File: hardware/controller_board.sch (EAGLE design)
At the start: 123 parts, among them J1 FRSKY-GIMBAL-FRYSKY, J11 USB-MICROA-AMPHENOL-10118192-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, J2 FRSKY-GIMBAL-FRYSKY, J3 USB-MINIB-EDAC-690-005-299-043, J4 AVR_SPI_PRG_6NS, J5 JUMPER-SMT_2_NC_PASTE_NO-SILK, J8 FRSKY-GIMBAL-2X-SERVO, J9 FRSKY-GIMBAL-2X-SERVO, P1 TEST-POINT, P2 TEST-POINT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

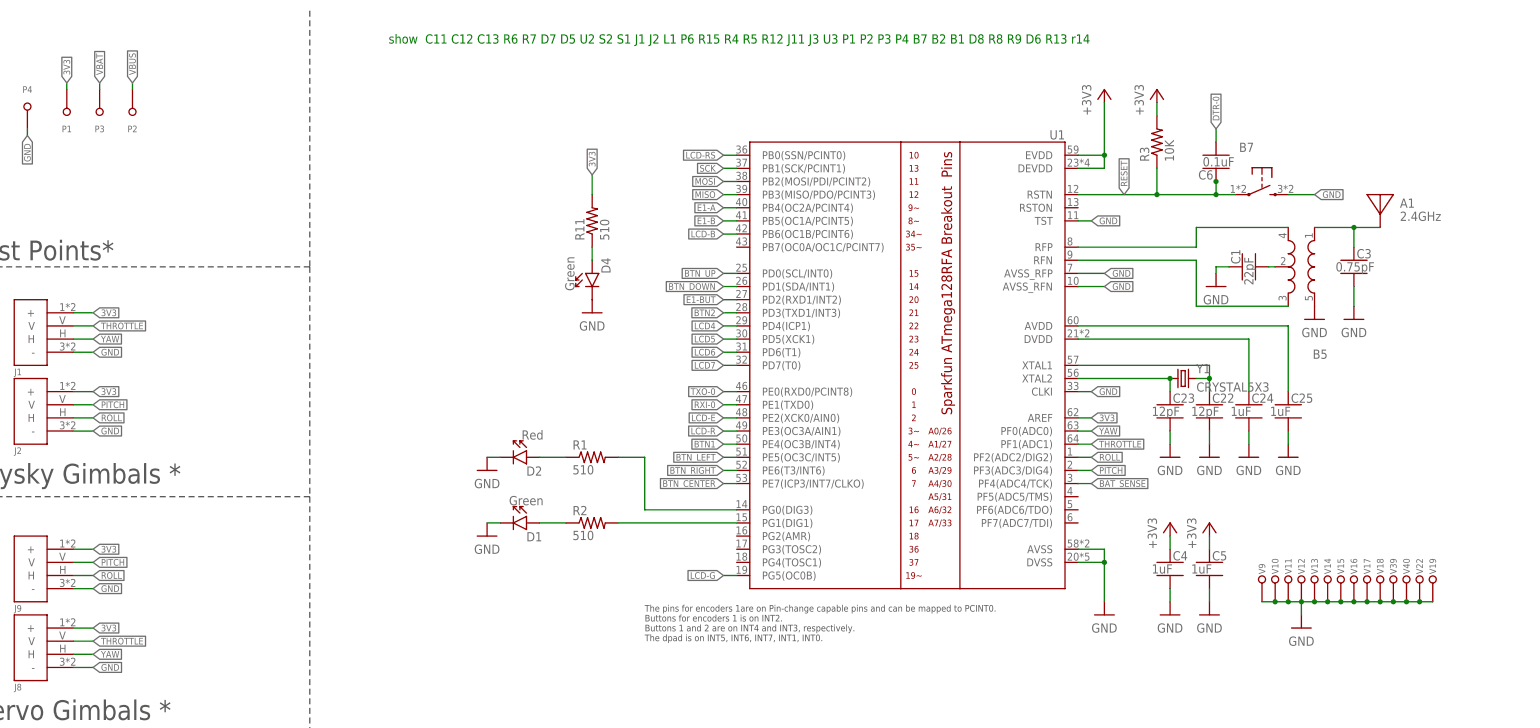
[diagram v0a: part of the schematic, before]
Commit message: added configuration jumpers for AREF
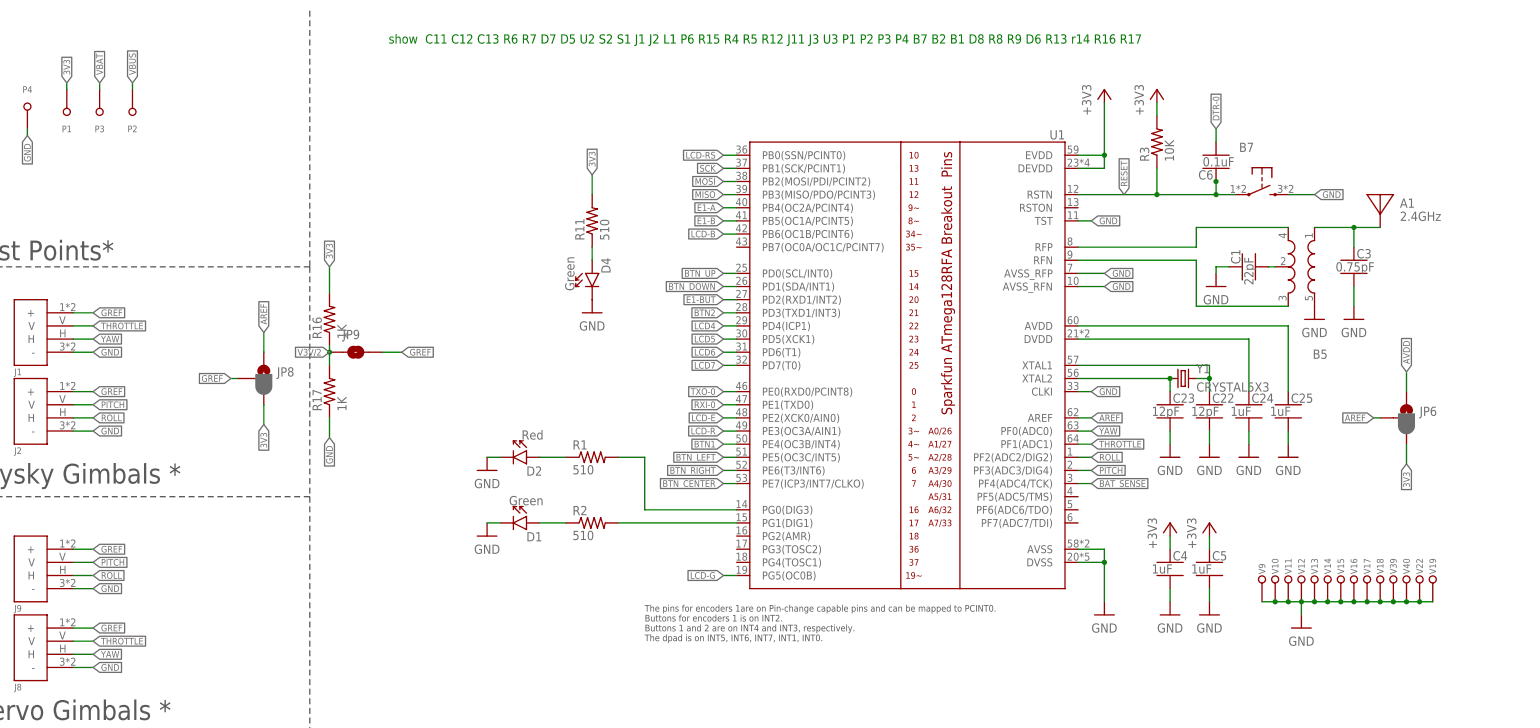
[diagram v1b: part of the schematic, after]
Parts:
- added JP6, JP8: JUMPER-SMT_3_1-NC_PASTE_NO-SILK, RemoteParts:JUMPER-SMT_3_1-NC_PASTE_NO-SILK
- added JP9: JUMPER-SMT_2_NO_NO-SILK, RemoteParts:JUMPER-SMT_2_NO_NO-SILK
- added R16, R17: 1K, quadparts_prebuilt:RESISTOR_SMD-2012-0805-1K
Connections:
- new net AREF: JP6.2, JP8.1, U1.AREF
- new net AVDD: JP6.1
- new net GREF: J1.+, J2.+, J8.+, J9.+, JP8.2, JP9.2
- new net V3V/2: JP9.1, R16.1, R17.2
- net 3V3: now also JP6.3, JP8.3, R16.2; no longer J1.+, J2.+, J8.+, J9.+, U1.AREF
- net GND: now also R17.1
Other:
- note added: "show C11 C12 C13 R6 R7 D7 D5 U2 S2 S1 J1 J2 L1 P6 R15 R4 R5 R12 J11 J3 U3 P1 P2 P3 P4 B7 B2 B1 D8 R8 R9 D6 R13 r14 R16 R17"
- note removed: "show C11 C12 C13 R6 R7 D7 D5 U2 S2 S1 J1 J2 L1 P6 R15 R4 R5 R12 J11 J3 U3 P1 P2 P3 P4 B7 B2 B1 D8 R8 R9 D6 R13 r14"
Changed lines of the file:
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@@
 <setting verticaltext="up"/>
 </settings>
-<grid distance="0.1" unitdist="inch" unit="inch" style="lines" multiple="1" display="no" altdistance="0.01" altunitdist="inch" altunit="inch"/>
+<grid distance="0.05" unitdist="inch" unit="inch" style="lines" multiple="1" display="no" altdistance="0.01" altunitdist="inch" altunit="inch"/>
 <layers>
 <layer number="99" name="SpiceOrder" color="7" fill="1" visible="no" active="no"/>
@@
 <part name="E1" library="RemoteParts" deviceset="ROTARY-ENCODER-W/BUTTON" device="-BOURNS-PEC12R-30MM"/>
 <part name="J5" library="RemoteParts" deviceset="JUMPER-SMT_2_NC_PASTE" device="_NO-SILK"/>
+<part name="JP6" library="RemoteParts" deviceset="JUMPER-SMT_3_1-NC_PASTE" device="_NO-SILK"/>
+<part name="JP8" library="RemoteParts" deviceset="JUMPER-SMT_3_1-NC_PASTE" device="_NO-SILK"/>
+<part name="R16" library="quadparts_prebuilt" deviceset="RESISTOR_" device="SMD-2012-0805-1K" value="1K"/>
+<part name="R17" library="quadparts_prebuilt" deviceset="RESISTOR_" device="SMD-2012-0805-1K" value="1K"/>
+<part name="JP9" library="RemoteParts" deviceset="JUMPER-SMT_2_NO" device="_NO-SILK"/>
 </parts>
 <sheets>
@@
 <wire x1="72.39" y1="96.52" x2="3.81" y2="95.25" width="0.1524" layer="97" style="longdash"/>
 <text x="6.35" y="97.79" size="3.81" layer="97">150mA 3.3V Regulator *</text>
-<text x="87.63" y="269.24" size="1.778" layer="91">show  C11 C12 C13 R6 R7 D7 D5 U2 S2 S1 J1 J2 L1 P6 R15 R4 R5 R12 J11 J3 U3 P1 P2 P3 P4 B7 B2 B1 D8 R8 R9 D6 R13 r14</text>
+<text x="87.63" y="269.24" size="1.778" layer="91">show  C11 C12 C13 R6 R7 D7 D5 U2 S2 S1 J1 J2 L1 P6 R15 R4 R5 R12 J11 J3 U3 P1 P2 P3 P4 B7 B2 B1 D8 R8 R9 D6 R13 r14 R16 R17</text>
 <text x="7.62" y="132.08" size="1.778" layer="97">C10 is the input cap (shared with lipo charger)</text>
 </plain>
@@
 <instance part="E1" gate="G$1" x="388.62" y="267.97"/>
 <instance part="J5" gate="G$1" x="21.59" y="107.95"/>
+<instance part="JP6" gate="G$1" x="284.48" y="196.85"/>
+<instance part="JP8" gate="G$1" x="63.5" y="204.47"/>
+<instance part="R16" gate="G$1" x="76.2" y="215.9" rot="R90"/>
+<instance part="R17" gate="G$1" x="76.2" y="201.93" rot="R90"/>
+<instance part="JP9" gate="G$1" x="81.28" y="209.55"/>
 </instances>
 <busses>
@@
 <label x="300.99" y="68.58" size="1.27" layer="95" xref="yes"/>
 </segment>
+<segment>
+<pinref part="R17" gate="G$1" pin="1"/>
+<wire x1="76.2" y1="196.85" x2="76.2" y2="193.04" width="0.1524" layer="91"/>
+<label x="76.2" y="193.04" size="1.27" layer="95" rot="R270" xref="yes"/>
+</segment>
 </net>
 <net name="BTN1" class="0">
@@
 </segment>
 <segment>
-<pinref part="U1" gate="G$1" pin="AREF"/>
-<wire x1="223.52" y1="196.85" x2="220.98" y2="196.85" width="0.1524" layer="91"/>
-<label x="223.52" y="196.85" size="1.27" layer="95" xref="yes"/>
-</segment>
-<segment>
 <wire x1="25.4" y1="261.62" x2="25.4" y2="260.35" width="0.1524" layer="91"/>
 <label x="25.4" y="261.62" size="1.27" layer="95" rot="R90" xref="yes"/>
 <pinref part="P1" gate="G$1" pin="T"/>
-</segment>
-<segment>
-<pinref part="J1" gate="G$1" pin="+"/>
-<wire x1="26.67" y1="217.17" x2="30.48" y2="217.17" width="0.1524" layer="91"/>
-<label x="30.48" y="217.17" size="1.27" layer="95" xref="yes"/>
-</segment>
-<segment>
-<pinref part="J8" gate="G$1" pin="+"/>
-<wire x1="26.67" y1="156.21" x2="30.48" y2="156.21" width="0.1524" layer="91"/>
-<label x="30.48" y="156.21" size="1.27" layer="95" xref="yes"/>
-</segment>
-<segment>
-<pinref part="J2" gate="G$1" pin="+"/>
-<wire x1="26.67" y1="201.93" x2="30.48" y2="201.93" width="0.1524" layer="91"/>
-<label x="30.48" y="201.93" size="1.27" layer="95" xref="yes"/>
-</segment>
-<segment>
-<pinref part="J9" gate="G$1" pin="+"/>
-<wire x1="26.67" y1="171.45" x2="30.48" y2="171.45" width="0.1524" layer="91"/>
-<label x="30.48" y="171.45" size="1.27" layer="95" xref="yes"/>
 </segment>
 <segment>
@@
 <wire x1="289.56" y1="73.66" x2="300.99" y2="73.66" width="0.1524" layer="91"/>
 <label x="300.99" y="73.66" size="1.27" layer="95" xref="yes"/>
+</segment>
+<segment>
+<pinref part="JP6" gate="G$1" pin="3"/>
+<wire x1="284.48" y1="191.77" x2="284.48" y2="187.96" width="0.1524" layer="91"/>
+<label x="284.48" y="187.96" size="1.27" layer="95" rot="R270" xref="yes"/>
+</segment>
+<segment>
+<pinref part="JP8" gate="G$1" pin="3"/>
+<wire x1="63.5" y1="199.39" x2="63.5" y2="195.58" width="0.1524" layer="91"/>
+<label x="63.5" y="195.58" size="1.27" layer="95" rot="R270" xref="yes"/>
+</segment>
+<segment>
+<pinref part="R16" gate="G$1" pin="2"/>
+<wire x1="76.2" y1="220.98" x2="76.2" y2="226.06" width="0.1524" layer="91"/>
+<label x="76.2" y="226.06" size="1.27" layer="95" rot="R90" xref="yes"/>
 </segment>
 </net>
@@
 </segment>
 </net>
+<net name="AREF" class="0">
+<segment>
+<pinref part="JP6" gate="G$1" pin="2"/>
+<wire x1="279.4" y1="196.85" x2="278.13" y2="196.85" width="0.1524" layer="91"/>
+<label x="278.13" y="196.85" size="1.27" layer="95" rot="R180" xref="yes"/>
+</segment>
+<segment>
+<pinref part="U1" gate="G$1" pin="AREF"/>
+<wire x1="223.52" y1="196.85" x2="220.98" y2="196.85" width="0.1524" layer="91"/>
+<label x="223.52" y="196.85" size="1.27" layer="95" xref="yes"/>
+</segment>
+<segment>
+<pinref part="JP8" gate="G$1" pin="1"/>
+<wire x1="63.5" y1="209.55" x2="63.5" y2="213.36" width="0.1524" layer="91"/>
+<label x="63.5" y="213.36" size="1.27" layer="95" rot="R90" xref="yes"/>
+</segment>
+</net>
+<net name="AVDD" class="0">
+<segment>
+<pinref part="JP6" gate="G$1" pin="1"/>
+<wire x1="284.48" y1="201.93" x2="284.48" y2="205.74" width="0.1524" layer="91"/>
+<label x="284.48" y="205.74" size="1.27" layer="95" rot="R90" xref="yes"/>
+</segment>
+</net>
+<net name="GREF" class="0">
+<segment>
+<pinref part="JP8" gate="G$1" pin="2"/>
+<wire x1="58.42" y1="204.47" x2="57.15" y2="204.47" width="0.1524" layer="91"/>
+<label x="57.15" y="204.47" size="1.27" layer="95" rot="R180" xref="yes"/>
+</segment>
+<segment>
+<pinref part="J1" gate="G$1" pin="+"/>
+<wire x1="26.67" y1="217.17" x2="30.48" y2="217.17" width="0.1524" layer="91"/>
+<label x="30.48" y="217.17" size="1.27" layer="95" xref="yes"/>
+</segment>
+<segment>
+<pinref part="J2" gate="G$1" pin="+"/>
+<wire x1="26.67" y1="201.93" x2="30.48" y2="201.93" width="0.1524" layer="91"/>
+<label x="30.48" y="201.93" size="1.27" layer="95" xref="yes"/>
+</segment>
+<segment>
+<pinref part="J9" gate="G$1" pin="+"/>
+<wire x1="26.67" y1="171.45" x2="30.48" y2="171.45" width="0.1524" layer="91"/>
+<label x="30.48" y="171.45" size="1.27" layer="95" xref="yes"/>
+</segment>
+<segment>
+<pinref part="J8" gate="G$1" pin="+"/>
+<wire x1="26.67" y1="156.21" x2="30.48" y2="156.21" width="0.1524" layer="91"/>
+<label x="30.48" y="156.21" size="1.27" layer="95" xref="yes"/>
+</segment>
+<segment>
+<pinref part="JP9" gate="G$1" pin="2"/>
+<wire x1="86.36" y1="209.55" x2="90.17" y2="209.55" width="0.1524" layer="91"/>
+<label x="90.17" y="209.55" size="1.27" layer="95" xref="yes"/>
+</segment>
+</net>
+<net name="V3V/2" class="0">
+<segment>
+<pinref part="R16" gate="G$1" pin="1"/>
+<pinref part="R17" gate="G$1" pin="2"/>
+<wire x1="76.2" y1="210.82" x2="76.2" y2="209.55" width="0.1524" layer="91"/>
+<pinref part="JP9" gate="G$1" pin="1"/>
+<wire x1="76.2" y1="209.55" x2="76.2" y2="207.01" width="0.1524" layer="91"/>
+<junction x="76.2" y="209.55"/>
+<label x="76.2" y="209.55" size="1.27" layer="95" rot="R180" xref="yes"/>
+</segment>
+</net>

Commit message: test solder jumpers
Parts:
- added JP10, JP11, JP12, JP13, JP14, JP15, JP16, JP17: JUMPER-SMT_3_0-NC_PASTE, RemoteParts:JUMPER-SMT_3_0-NC_PASTE
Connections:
- new net N$1: JP10.3, JP11.1
- new net N$18: JP11.3, JP12.1
- new net N$25: JP12.3, JP13.1
- new net N$26: JP13.3, JP14.1
- new net N$27: JP14.3, JP15.1
- new net N$28: JP15.3, JP16.1
- new net N$29: JP16.3, JP17.1
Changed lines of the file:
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@@
 <part name="R17" library="quadparts_prebuilt" deviceset="RESISTOR_" device="SMD-2012-0805-1K" value="1K"/>
 <part name="JP9" library="RemoteParts" deviceset="JUMPER-SMT_2_NO" device="_NO-SILK"/>
+<part name="JP10" library="RemoteParts" deviceset="JUMPER-SMT_3_0-NC_PASTE" device=""/>
+<part name="JP11" library="RemoteParts" deviceset="JUMPER-SMT_3_0-NC_PASTE" device=""/>
+<part name="JP12" library="RemoteParts" deviceset="JUMPER-SMT_3_0-NC_PASTE" device=""/>
+<part name="JP13" library="RemoteParts" deviceset="JUMPER-SMT_3_0-NC_PASTE" device=""/>
+<part name="JP14" library="RemoteParts" deviceset="JUMPER-SMT_3_0-NC_PASTE" device=""/>
+<part name="JP15" library="RemoteParts" deviceset="JUMPER-SMT_3_0-NC_PASTE" device=""/>
+<part name="JP16" library="RemoteParts" deviceset="JUMPER-SMT_3_0-NC_PASTE" device=""/>
+<part name="JP17" library="RemoteParts" deviceset="JUMPER-SMT_3_0-NC_PASTE" device=""/>
 </parts>
 <sheets>
@@
 <instance part="R17" gate="G$1" x="76.2" y="201.93" rot="R90"/>
 <instance part="JP9" gate="G$1" x="81.28" y="209.55"/>
+<instance part="JP10" gate="G$1" x="29.21" y="86.36"/>
+<instance part="JP11" gate="G$1" x="29.21" y="76.2"/>
+<instance part="JP12" gate="G$1" x="29.21" y="66.04"/>
+<instance part="JP13" gate="G$1" x="29.21" y="55.88"/>
+<instance part="JP14" gate="G$1" x="29.21" y="45.72"/>
+<instance part="JP15" gate="G$1" x="29.21" y="35.56"/>
+<instance part="JP16" gate="G$1" x="29.21" y="25.4"/>
+<instance part="JP17" gate="G$1" x="29.21" y="15.24"/>
 </instances>
 <busses>
@@
 </segment>
 </net>
+<net name="N$1" class="0">
+<segment>
+<pinref part="JP10" gate="G$1" pin="3"/>
+<pinref part="JP11" gate="G$1" pin="1"/>
+</segment>
+</net>
+<net name="N$18" class="0">
+<segment>
+<pinref part="JP11" gate="G$1" pin="3"/>
+<pinref part="JP12" gate="G$1" pin="1"/>
+</segment>
+</net>
+<net name="N$25" class="0">
+<segment>
+<pinref part="JP12" gate="G$1" pin="3"/>
+<pinref part="JP13" gate="G$1" pin="1"/>
+</segment>
+</net>
+<net name="N$26" class="0">
+<segment>
+<pinref part="JP13" gate="G$1" pin="3"/>
+<pinref part="JP14" gate="G$1" pin="1"/>
+</segment>
+</net>
+<net name="N$27" class="0">
+<segment>
+<pinref part="JP14" gate="G$1" pin="3"/>
+<pinref part="JP15" gate="G$1" pin="1"/>
+</segment>
+</net>
+<net name="N$28" class="0">
+<segment>
+<pinref part="JP15" gate="G$1" pin="3"/>
+<pinref part="JP16" gate="G$1" pin="1"/>
+</segment>
+</net>
+<net name="N$29" class="0">
+<segment>
+<pinref part="JP16" gate="G$1" pin="3"/>
+<pinref part="JP17" gate="G$1" pin="1"/>
+</segment>
+</net>
